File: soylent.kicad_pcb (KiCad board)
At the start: 2 copper layers, 34.5 x 43.2 mm, 23 parts, among them J1 DB9_Female, J2 Conn_01x04, J3 Conn_01x04, J4 Conn_02x03_Counter_Clockwise, Q1 BC847BPN, Q2 BC847BPN, U1 ATtiny202-SS, U2 MIC5504-3.3YM5

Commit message: Ground plane fixups
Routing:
- net /RTS: track 14.9 -> 10.6 mm
- net /DTR: track 10.1 -> 13.0 mm
- net Net-(D1-Pad1): track 13.9 -> 15.0 mm
- net GND: vias 3 -> 2
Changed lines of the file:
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@@
     (thickness 1.6)
     (drawings 6)
-    (tracks 158)
+    (tracks 166)
     (zones 0)
     (modules 23)
@@
   (segment (start 228.0258 37.3126) (end 226.1108 39.2276) (width 0.25) (layer B.Cu) (net 1))
   (segment (start 234.5944 37.3126) (end 228.0258 37.3126) (width 0.25) (layer B.Cu) (net 1))
-  (via (at 242.824 51.054) (size 0.8) (drill 0.4) (layers F.Cu B.Cu) (net 1))
   (via (at 234.5944 34.7726) (size 0.8) (drill 0.4) (layers F.Cu B.Cu) (net 2))
   (segment (start 226.7358 34.7726) (end 226.1108 34.1476) (width 0.25) (layer B.Cu) (net 2))
@@
   (segment (start 232.8263 47.6913) (end 233.3696 47.6913) (width 0.25) (layer F.Cu) (net 2))
   (segment (start 233.3696 47.6913) (end 232.6696 47.6913) (width 0.25) (layer F.Cu) (net 2))
-  (segment (start 241.554 54.356) (end 241.9972 54.356) (width 0.25) (layer F.Cu) (net 2))
-  (segment (start 239.97899 55.93101) (end 241.554 54.356) (width 0.25) (layer F.Cu) (net 2))
+  (segment (start 241.7064 54.356) (end 241.9972 54.356) (width 0.25) (layer F.Cu) (net 2))
+  (segment (start 232.6696 47.6913) (end 231.3432 49.0177) (width 0.25) (layer F.Cu) (net 2))
   (segment (start 231.3432 54.9656) (end 232.30861 55.93101) (width 0.25) (layer F.Cu) (net 2))
-  (segment (start 232.30861 55.93101) (end 239.97899 55.93101) (width 0.25) (layer F.Cu) (net 2))
+  (segment (start 232.30861 55.93101) (end 240.13139 55.93101) (width 0.25) (layer F.Cu) (net 2))
   (segment (start 231.3432 49.0177) (end 231.3432 54.9656) (width 0.25) (layer F.Cu) (net 2))
-  (segment (start 232.6696 47.6913) (end 231.3432 49.0177) (width 0.25) (layer F.Cu) (net 2))
+  (segment (start 240.13139 55.93101) (end 241.7064 54.356) (width 0.25) (layer F.Cu) (net 2))
   (via (at 243.9416 37.3126) (size 0.8) (drill 0.4) (layers F.Cu B.Cu) (net 3))
   (segment (start 242.3922 37.3126) (end 243.9416 37.3126) (width 0.25) (layer F.Cu) (net 3))
@@
   (segment (start 248.958 41.1988) (end 248.008 42.1488) (width 0.25) (layer F.Cu) (net 8))
   (segment (start 248.958 41.1988) (end 248.958 44.7548) (width 0.25) (layer F.Cu) (net 8))
-  (segment (start 240.527794 50.192872) (end 241.026866 49.6938) (width 0.25) (layer F.Cu) (net 9))
-  (segment (start 240.527794 54.720408) (end 240.527794 50.192872) (width 0.25) (layer F.Cu) (net 9))
-  (segment (start 239.767201 55.481001) (end 240.527794 54.720408) (width 0.25) (layer F.Cu) (net 9))
-  (segment (start 237.582201 55.481001) (end 239.767201 55.481001) (width 0.25) (layer F.Cu) (net 9))
-  (segment (start 236.4572 54.356) (end 237.582201 55.481001) (width 0.25) (layer F.Cu) (net 9))
-  (segment (start 243.922201 58.321001) (end 247.4468 54.796402) (width 0.25) (layer F.Cu) (net 10))
-  (segment (start 241.737201 58.321001) (end 243.922201 58.321001) (width 0.25) (layer F.Cu) (net 10))
-  (segment (start 240.6122 57.196) (end 241.737201 58.321001) (width 0.25) (layer F.Cu) (net 10))
-  (segment (start 247.4468 52.2026) (end 244.938 49.6938) (width 0.25) (layer F.Cu) (net 10))
-  (segment (start 247.4468 54.796402) (end 247.4468 52.2026) (width 0.25) (layer F.Cu) (net 10))
+  (segment (start 236.4572 54.356) (end 237.5822 55.481) (width 0.25) (layer F.Cu) (net 9))
+  (segment (start 239.921 55.481) (end 240.5888 54.8132) (width 0.25) (layer F.Cu) (net 9))
+  (segment (start 237.5822 55.481) (end 239.921 55.481) (width 0.25) (layer F.Cu) (net 9))
+  (segment (start 240.5888 54.099398) (end 241.457199 53.230999) (width 0.25) (layer F.Cu) (net 9))
+  (segment (start 240.5888 54.8132) (end 240.5888 54.099398) (width 0.25) (layer F.Cu) (net 9))
+  (segment (start 242.374201 53.230999) (end 242.88199 52.72321) (width 0.25) (layer F.Cu) (net 9))
+  (segment (start 241.457199 53.230999) (end 242.374201 53.230999) (width 0.25) (layer F.Cu) (net 9))
+  (segment (start 242.88199 52.72321) (end 242.88199 50.19759) (width 0.25) (layer F.Cu) (net 9))
+  (segment (start 242.3782 49.6938) (end 241.026866 49.6938) (width 0.25) (layer F.Cu) (net 9))
+  (segment (start 242.88199 50.19759) (end 242.3782 49.6938) (width 0.25) (layer F.Cu) (net 9))
+  (segment (start 240.6122 56.3138) (end 240.6122 57.196) (width 0.25) (layer F.Cu) (net 10))
+  (segment (start 241.451099 55.474901) (end 240.6122 56.3138) (width 0.25) (layer F.Cu) (net 10))
+  (segment (start 242.537201 55.481001) (end 241.457199 55.481001) (width 0.25) (layer F.Cu) (net 10))
+  (segment (start 243.332 50.1904) (end 243.332 54.686202) (width 0.25) (layer F.Cu) (net 10))
+  (segment (start 241.457199 55.481001) (end 241.451099 55.474901) (width 0.25) (layer F.Cu) (net 10))
+  (segment (start 243.8286 49.6938) (end 243.332 50.1904) (width 0.25) (layer F.Cu) (net 10))
+  (segment (start 243.332 54.686202) (end 242.537201 55.481001) (width 0.25) (layer F.Cu) (net 10))
+  (segment (start 244.938 49.6938) (end 243.8286 49.6938) (width 0.25) (layer F.Cu) (net 10))
   (segment (start 236.6922 23.129) (end 236.6922 22.7076) (width 0.25) (layer F.Cu) (net 11))
   (segment (start 237.5916 24.0284) (end 236.6922 23.129) (width 0.25) (layer F.Cu) (net 11))
@@
   (segment (start 244.7036 26.439998) (end 242.292002 24.0284) (width 0.25) (layer F.Cu) (net 11))
   (segment (start 244.7036 27.5004) (end 244.7036 26.439998) (width 0.25) (layer F.Cu) (net 11))
-  (segment (start 241.601866 47.9438) (end 244.938 47.9438) (width 0.25) (layer F.Cu) (net 12))
-  (segment (start 241.026866 47.9438) (end 241.601866 47.9438) (width 0.25) (layer F.Cu) (net 12))
   (segment (start 249.7708 42.0838) (end 249.7708 41.1988) (width 0.25) (layer F.Cu) (net 12))
   (segment (start 249.80801 45.2253) (end 249.80801 42.12101) (width 0.25) (layer F.Cu) (net 12))
@@
   (segment (start 247.08951 47.9438) (end 249.80801 45.2253) (width 0.25) (layer F.Cu) (net 12))
   (segment (start 244.938 47.9438) (end 247.08951 47.9438) (width 0.25) (layer F.Cu) (net 12))
+  (segment (start 241.026866 47.9438) (end 242.308266 49.2252) (width 0.25) (layer F.Cu) (net 12))
+  (segment (start 243.6566 49.2252) (end 244.938 47.9438) (width 0.25) (layer F.Cu) (net 12))
+  (segment (start 242.308266 49.2252) (end 243.6566 49.2252) (width 0.25) (layer F.Cu) (net 12))
   (via (at 243.9416 36.0426) (size 0.8) (drill 0.4) (layers F.Cu B.Cu) (net 13))
   (segment (start 242.3922 36.0426) (end 243.9416 36.0426) (width 0.25) (layer F.Cu) (net 13))

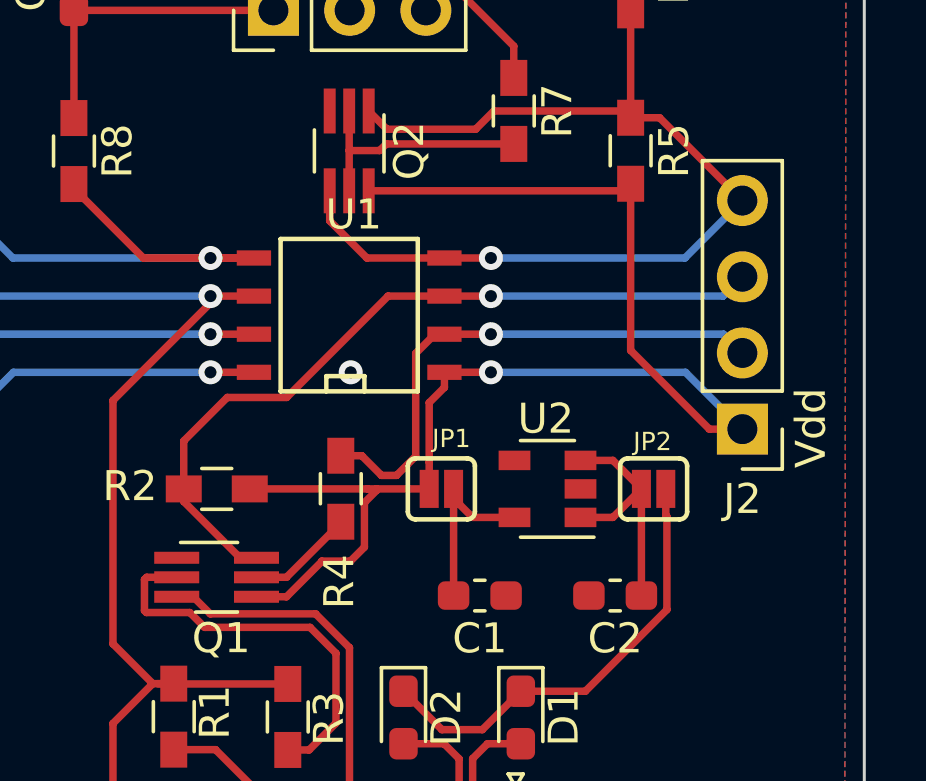
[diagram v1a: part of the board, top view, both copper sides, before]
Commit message: Reroute, no extraneous vias
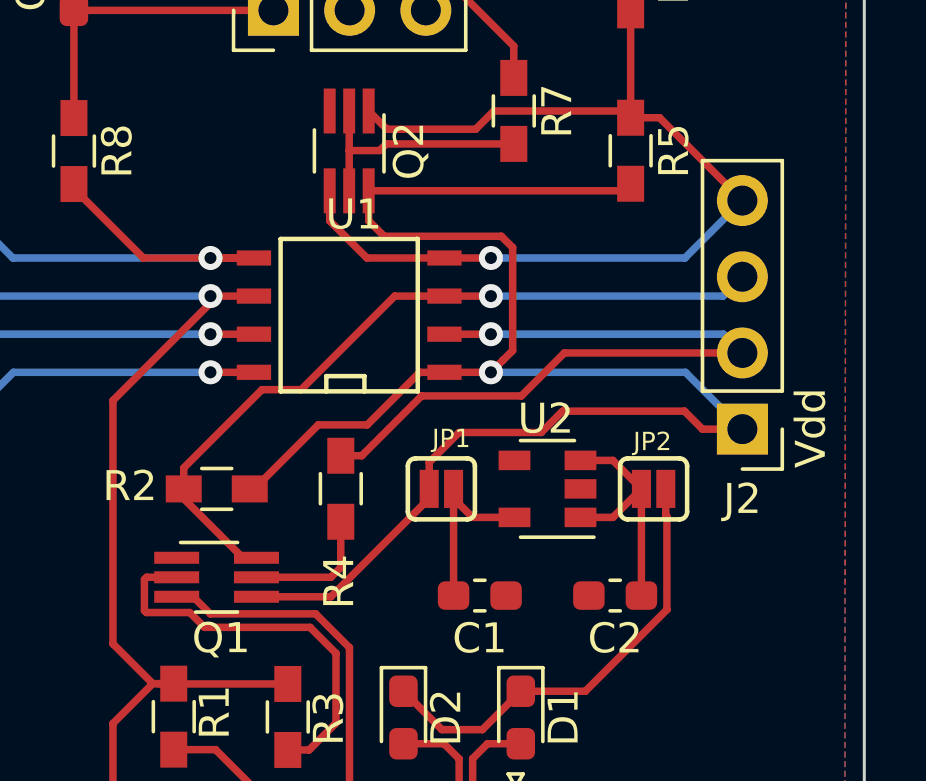
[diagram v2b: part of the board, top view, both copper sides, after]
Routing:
- net VDD: track 46.4 -> 58.0 mm
- net /PA6: track 17.9 -> 25.1 mm
- net Net-(Q1-Pad5): track 3.60 -> 4.47 mm
- net /PA7: track 26.1 -> 25.5 mm
- net GND: vias 2 -> 1
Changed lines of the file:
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@@
     (thickness 1.6)
     (drawings 6)
-    (tracks 166)
+    (tracks 169)
     (zones 0)
     (modules 23)
@@
   )
   (via (at 234.5944 37.3126) (size 0.8) (drill 0.4) (layers F.Cu B.Cu) (net 1))
-  (via (at 239.268 37.3126) (size 0.8) (drill 0.4) (layers F.Cu B.Cu) (net 1))
   (segment (start 236.0422 37.3126) (end 234.5944 37.3126) (width 0.25) (layer F.Cu) (net 1))
   (segment (start 228.0258 37.3126) (end 226.1108 39.2276) (width 0.25) (layer B.Cu) (net 1))
@@
   (segment (start 250.4286 37.3126) (end 252.3236 39.2076) (width 0.25) (layer B.Cu) (net 3))
   (segment (start 243.9416 37.3126) (end 250.4286 37.3126) (width 0.25) (layer B.Cu) (net 3))
-  (segment (start 238.3028 43.62) (end 238.3028 43.60641) (width 0.25) (layer F.Cu) (net 3))
-  (segment (start 237.1276 44.7952) (end 238.3028 43.62) (width 0.25) (layer F.Cu) (net 3))
-  (segment (start 236.1276 44.7952) (end 237.1276 44.7952) (width 0.25) (layer F.Cu) (net 3))
-  (segment (start 239.259592 43.60641) (end 239.7252 43.140802) (width 0.25) (layer F.Cu) (net 3))
-  (segment (start 238.3028 43.60641) (end 239.259592 43.60641) (width 0.25) (layer F.Cu) (net 3))
-  (segment (start 235.9026 41.1988) (end 239.8268 41.1988) (width 0.25) (layer F.Cu) (net 3))
-  (segment (start 241.8842 38.3246) (end 241.8842 40.3138) (width 0.25) (layer F.Cu) (net 3))
-  (segment (start 242.3922 37.8166) (end 241.8842 38.3246) (width 0.25) (layer F.Cu) (net 3))
-  (segment (start 241.8842 40.3138) (end 241.8842 41.1988) (width 0.25) (layer F.Cu) (net 3))
-  (segment (start 242.3922 37.3126) (end 242.3922 37.8166) (width 0.25) (layer F.Cu) (net 3))
-  (segment (start 240.1316 41.2496) (end 239.7252 41.656) (width 0.25) (layer F.Cu) (net 3))
-  (segment (start 240.1316 41.1988) (end 240.1316 41.2496) (width 0.25) (layer F.Cu) (net 3))
-  (segment (start 239.7252 41.656) (end 239.7252 43.140802) (width 0.25) (layer F.Cu) (net 3))
-  (segment (start 239.8268 41.1988) (end 240.1316 41.1988) (width 0.25) (layer F.Cu) (net 3))
-  (segment (start 240.1316 41.1988) (end 241.8842 41.1988) (width 0.25) (layer F.Cu) (net 3))
   (segment (start 248.3642 31.2626) (end 248.5992 31.0276) (width 0.25) (layer F.Cu) (net 3))
   (segment (start 239.8672 31.2626) (end 248.3642 31.2626) (width 0.25) (layer F.Cu) (net 3))
-  (segment (start 251.2236 39.2076) (end 252.3236 39.2076) (width 0.25) (layer F.Cu) (net 3))
-  (segment (start 248.5992 36.5832) (end 251.2236 39.2076) (width 0.25) (layer F.Cu) (net 3))
-  (segment (start 248.5992 31.0276) (end 248.5992 36.5832) (width 0.25) (layer F.Cu) (net 3))
+  (segment (start 241.8842 41.5163) (end 241.8842 41.1988) (width 0.25) (layer F.Cu) (net 3))
+  (segment (start 238.6053 44.7952) (end 241.8842 41.5163) (width 0.25) (layer F.Cu) (net 3))
+  (segment (start 236.1276 44.7952) (end 238.6053 44.7952) (width 0.25) (layer F.Cu) (net 3))
+  (segment (start 241.5707 37.3126) (end 242.3922 37.3126) (width 0.25) (layer F.Cu) (net 3))
+  (segment (start 239.8181 39.0652) (end 241.5707 37.3126) (width 0.25) (layer F.Cu) (net 3))
+  (segment (start 236.0526 41.1988) (end 238.1862 39.0652) (width 0.25) (layer F.Cu) (net 3))
+  (segment (start 238.1862 39.0652) (end 239.8181 39.0652) (width 0.25) (layer F.Cu) (net 3))
+  (segment (start 235.9026 41.1988) (end 236.0526 41.1988) (width 0.25) (layer F.Cu) (net 3))
+  (segment (start 244.341599 36.912601) (end 243.9416 37.3126) (width 0.25) (layer F.Cu) (net 3))
+  (segment (start 244.666601 36.587599) (end 244.341599 36.912601) (width 0.25) (layer F.Cu) (net 3))
+  (segment (start 244.666601 33.154599) (end 244.666601 36.587599) (width 0.25) (layer F.Cu) (net 3))
+  (segment (start 240.382199 32.777599) (end 244.289601 32.777599) (width 0.25) (layer F.Cu) (net 3))
+  (segment (start 244.289601 32.777599) (end 244.666601 33.154599) (width 0.25) (layer F.Cu) (net 3))
+  (segment (start 239.8672 32.2626) (end 240.382199 32.777599) (width 0.25) (layer F.Cu) (net 3))
+  (segment (start 239.8672 31.2626) (end 239.8672 32.2626) (width 0.25) (layer F.Cu) (net 3))
+  (segment (start 245.618 39.3192) (end 246.3292 38.608) (width 0.25) (layer F.Cu) (net 3))
+  (segment (start 241.8842 41.1988) (end 241.8842 40.3138) (width 0.25) (layer F.Cu) (net 3))
+  (segment (start 241.8842 40.3138) (end 242.8788 39.3192) (width 0.25) (layer F.Cu) (net 3))
+  (segment (start 246.3292 38.608) (end 250.3932 38.608) (width 0.25) (layer F.Cu) (net 3))
+  (segment (start 242.8788 39.3192) (end 245.618 39.3192) (width 0.25) (layer F.Cu) (net 3))
+  (segment (start 250.9928 39.2076) (end 252.3236 39.2076) (width 0.25) (layer F.Cu) (net 3))
+  (segment (start 250.3932 38.608) (end 250.9928 39.2076) (width 0.25) (layer F.Cu) (net 3))
   (segment (start 234.7625 49.8913) (end 233.3696 49.8913) (width 0.25) (layer F.Cu) (net 4))
   (segment (start 239.2272 54.356) (end 234.7625 49.8913) (width 0.25) (layer F.Cu) (net 4))
@@
   (segment (start 237.8807 49.9013) (end 238.77719 49.00481) (width 0.25) (layer F.Cu) (net 5))
   (segment (start 237.170733 49.9013) (end 237.8807 49.9013) (width 0.25) (layer F.Cu) (net 5))
-  (segment (start 238.9372 42.3356) (end 238.9372 42.2938) (width 0.25) (layer F.Cu) (net 6))
-  (segment (start 237.1276 44.1452) (end 238.9372 42.3356) (width 0.25) (layer F.Cu) (net 6))
-  (segment (start 236.1276 44.1452) (end 237.1276 44.1452) (width 0.25) (layer F.Cu) (net 6))
+  (segment (start 238.6076 44.1452) (end 238.9372 43.8156) (width 0.25) (layer F.Cu) (net 6))
+  (segment (start 238.9372 43.8156) (end 238.9372 42.2938) (width 0.25) (layer F.Cu) (net 6))
+  (segment (start 236.1276 44.1452) (end 238.6076 44.1452) (width 0.25) (layer F.Cu) (net 6))
   (segment (start 242.697 41.5163) (end 242.697 41.1988) (width 0.25) (layer F.Cu) (net 7))
   (segment (start 243.3295 42.1488) (end 242.697 41.5163) (width 0.25) (layer F.Cu) (net 7))
@@
   (segment (start 251.6986 36.0426) (end 252.3236 36.6676) (width 0.25) (layer B.Cu) (net 13))
   (segment (start 243.9416 36.0426) (end 251.6986 36.0426) (width 0.25) (layer B.Cu) (net 13))
-  (segment (start 242.0747 36.0426) (end 242.3922 36.0426) (width 0.25) (layer F.Cu) (net 13))
-  (segment (start 241.43419 40.111308) (end 241.43419 36.68311) (width 0.25) (layer F.Cu) (net 13))
-  (segment (start 240.29219 40.74879) (end 240.796708 40.74879) (width 0.25) (layer F.Cu) (net 13))
-  (segment (start 240.796708 40.74879) (end 241.43419 40.111308) (width 0.25) (layer F.Cu) (net 13))
-  (segment (start 239.6372 40.0938) (end 240.29219 40.74879) (width 0.25) (layer F.Cu) (net 13))
-  (segment (start 241.43419 36.68311) (end 242.0747 36.0426) (width 0.25) (layer F.Cu) (net 13))
+  (segment (start 252.2828 36.6268) (end 252.3236 36.6676) (width 0.25) (layer F.Cu) (net 13))
+  (segment (start 241.631 38.1) (end 244.9576 38.1) (width 0.25) (layer F.Cu) (net 13))
+  (segment (start 239.6372 40.0938) (end 241.631 38.1) (width 0.25) (layer F.Cu) (net 13))
   (segment (start 238.9372 40.0938) (end 239.6372 40.0938) (width 0.25) (layer F.Cu) (net 13))
+  (segment (start 246.39 36.6676) (end 252.3236 36.6676) (width 0.25) (layer F.Cu) (net 13))
+  (segment (start 244.9576 38.1) (end 246.39 36.6676) (width 0.25) (layer F.Cu) (net 13))
   (via (at 243.9416 34.7726) (size 0.8) (drill 0.4) (layers F.Cu B.Cu) (net 14))
-  (segment (start 233.7026 41.6202) (end 233.7026 41.1988) (width 0.25) (layer F.Cu) (net 14))
-  (segment (start 235.5776 43.4952) (end 233.7026 41.6202) (width 0.25) (layer F.Cu) (net 14))
-  (segment (start 236.1276 43.4952) (end 235.5776 43.4952) (width 0.25) (layer F.Cu) (net 14))
-  (segment (start 240.5126 34.7726) (end 242.3922 34.7726) (width 0.25) (layer F.Cu) (net 14))
-  (segment (start 237.1344 38.1508) (end 240.5126 34.7726) (width 0.25) (layer F.Cu) (net 14))
-  (segment (start 235.1532 38.1508) (end 237.1344 38.1508) (width 0.25) (layer F.Cu) (net 14))
-  (segment (start 233.7026 39.6014) (end 235.1532 38.1508) (width 0.25) (layer F.Cu) (net 14))
-  (segment (start 233.7026 41.1988) (end 233.7026 39.6014) (width 0.25) (layer F.Cu) (net 14))
   (segment (start 242.3922 34.7726) (end 243.9416 34.7726) (width 0.25) (layer F.Cu) (net 14))
   (segment (start 251.6786 34.7726) (end 252.3236 34.1276) (width 0.25) (layer B.Cu) (net 14))
   (segment (start 243.9416 34.7726) (end 251.6786 34.7726) (width 0.25) (layer B.Cu) (net 14))
+  (segment (start 241.5707 34.7726) (end 242.3922 34.7726) (width 0.25) (layer F.Cu) (net 14))
+  (segment (start 236.309799 37.891601) (end 237.615997 37.891601) (width 0.25) (layer F.Cu) (net 14))
+  (segment (start 240.734998 34.7726) (end 241.5707 34.7726) (width 0.25) (layer F.Cu) (net 14))
+  (segment (start 233.7026 40.4988) (end 236.309799 37.891601) (width 0.25) (layer F.Cu) (net 14))
+  (segment (start 237.615997 37.891601) (end 240.734998 34.7726) (width 0.25) (layer F.Cu) (net 14))
+  (segment (start 233.7026 41.1988) (end 233.7026 40.4988) (width 0.25) (layer F.Cu) (net 14))
+  (segment (start 233.7026 41.5262) (end 233.7026 41.1988) (width 0.25) (layer F.Cu) (net 14))
+  (segment (start 235.6716 43.4952) (end 233.7026 41.5262) (width 0.25) (layer F.Cu) (net 14))
+  (segment (start 236.1276 43.4952) (end 235.6716 43.4952) (width 0.25) (layer F.Cu) (net 14))
   (via (at 243.9416 33.5026) (size 0.8) (drill 0.4) (layers F.Cu B.Cu) (net 15))
   (segment (start 242.3922 33.5026) (end 243.9416 33.5026) (width 0.25) (layer F.Cu) (net 15))

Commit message: Cosmetic rerouting
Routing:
- net /TD: track 49.6 -> 60.6 mm
- net /RD: track 22.0 -> 18.5 mm
- net Net-(Q1-Pad2): track 13.4 -> 10.3 mm
- net /DTR: track 13.0 -> 10.1 mm
- net Net-(D1-Pad1): track 15.0 -> 16.9 mm

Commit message: Rename pads
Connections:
- net /PA1 renamed /WIN
- net /PA2 renamed /WOUT
- net /PA6 renamed /TX
- net /PA7 renamed /RX
